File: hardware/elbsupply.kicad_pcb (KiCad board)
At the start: 2 copper layers, 105 x 64.4 mm, 86 parts, among them CON1 AVR-ISP-6, IC1 ATMEGA8-AI, M3 Screw_PAN_Head_M3, P1 OUT_POS, P2 OUT_GND, P3 POWER_IN, Q1 KST2907A, SW1 SW_L, SW2 SW_R, SW3 SW_OE, SW4 SW_MD, U1 LM393, U2 TPS54331DDA, U3 LT1490, U4 LM358, U5 TS78L05CS, U6 LT3083

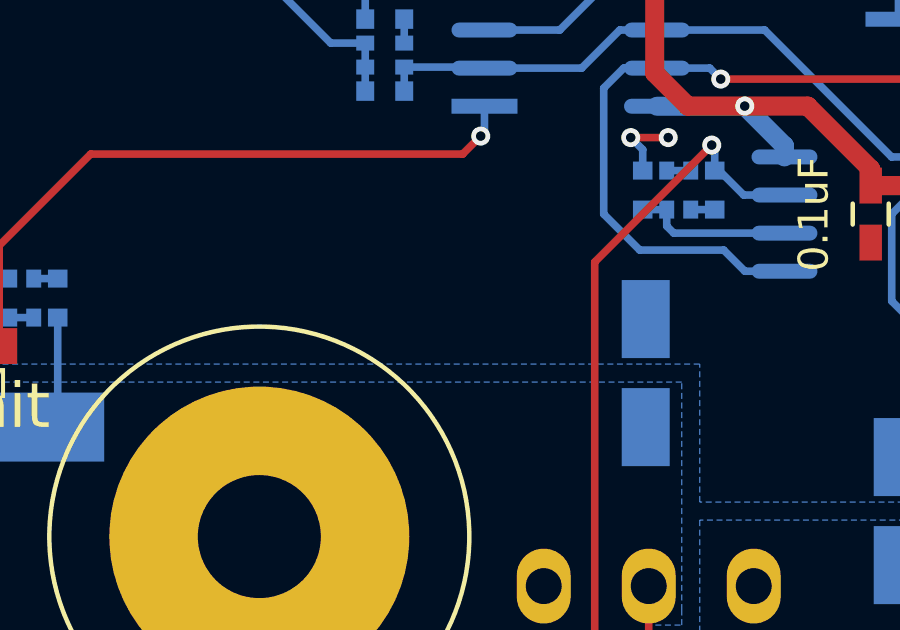
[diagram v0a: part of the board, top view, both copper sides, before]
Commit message: quickly added LM334 constant current sink to ensure stable operation of LT3083
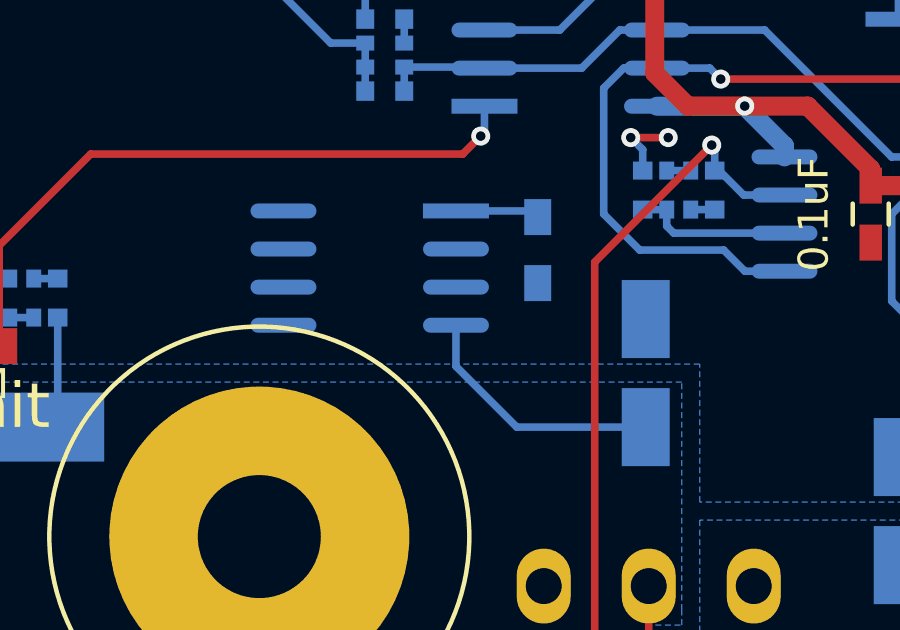
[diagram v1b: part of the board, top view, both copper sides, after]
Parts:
- added R26: R, Resistors_SMD:R_0603_HandSoldering, B.Cu at (80.4, 73.0)
- added U7: LM334, devthrash_KICAD:SO8, B.Cu at (74.8, 73.6)
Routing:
- net /LIN_OUT: track 37.8 -> 46.3 mm
- net Net-(R26-Pad1): track 0.00 -> 2.81 mm

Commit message: started new layout
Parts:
- added C28: 1uF, Capacitors_SMD:C_0805_HandSoldering, B.Cu at (101.4, 172.1)
- added D6: LM4040, Housings_SOT-23_SOT-143_TSOT-6:SOT-23_Handsoldering, B.Cu at (74.1, 60.7)
- added D7: SK34A, SMD_Packages:DO-214-AC_SMA, F.Cu at (63.6, 108.0)
- added D8: SK34A, SMD_Packages:DO-214-AC_SMA, B.Cu at (61.7, 82.7)
- added HS1: HEATSINK V5640A, devthrash:Heatsink-V5640A, B.Cu at (71.1, 77.7)
- added L2: 220uH, devthrash:242418FPS-Fastron, B.Cu at (115.4, 63.9)
- added Q2: KST2907A, Housings_SOT-23_SOT-143_TSOT-6:SOT-23_Handsoldering, B.Cu at (181.5, 107.1)
- added Q3: IRLML6302, Housings_SOT-23_SOT-143_TSOT-6:SOT-23_Handsoldering, B.Cu at (185.3, 107.1)
- added Q4: 2N2222A, Housings_SOT-23_SOT-143_TSOT-6:SOT-23_Handsoldering, B.Cu at (101.8, 169.2)
- added Q5: 2N2222A, Housings_SOT-23_SOT-143_TSOT-6:SOT-23_Handsoldering, F.Cu at (73.4, 117.0)
- added R27: 10k, Resistors_SMD:R_0603_HandSoldering, F.Cu at (63.1, 135.5)
- added R28: 10k, Resistors_SMD:R_0603_HandSoldering, F.Cu at (70.2, 138.9)
- added R29: 10k, Resistors_SMD:R_0603_HandSoldering, F.Cu at (73.5, 144.0)
- added RP6: 10k, devthrash:YC164-Yageo-Handsoldering, B.Cu at (98.5, 162.8)
- added RP7: 10k, devthrash:YC164-Yageo-Handsoldering, B.Cu at (102.6, 162.8)
- C10: value 10nF -> 120pF
- C11: value 10nF -> 10uF; footprint Capacitors_SMD:C_0603_HandSoldering -> Capacitors_SMD:c_elec_4x4.5
- C12: value 10nF -> 10uF; footprint Capacitors_SMD:C_0603_HandSoldering -> Capacitors_SMD:C_0805_HandSoldering
- C13, C17, C18, C19, C23: footprint Capacitors_SMD:C_0603_HandSoldering -> Capacitors_SMD:C_0805_HandSoldering
- C14, C21: value 0.1uF -> 1uF; footprint Capacitors_SMD:C_0603_HandSoldering -> Capacitors_SMD:C_0805_HandSoldering
- C20: value 10uF -> 1uF; footprint Capacitors_SMD:c_elec_4x4.5 -> Capacitors_SMD:C_0805_HandSoldering; moved to F.Cu
- C22: footprint Capacitors_SMD:C_0603_HandSoldering -> Capacitors_SMD:C_0805_HandSoldering; moved to B.Cu
- C25: moved to B.Cu
- C26, R3: moved to F.Cu
- C4: value 7pF -> 22pF
- C7, C9: value 10nF -> 0.1uF; footprint Capacitors_SMD:C_0603_HandSoldering -> Capacitors_SMD:C_0805_HandSoldering
- D5: value SM6T27A -> SK34A; footprint Diodes_SMD:Diode-SMB_Handsoldering -> SMD_Packages:DO-214-AC_SMA
- DS1: footprint devthrash_KICAD:LCD16X2 -> devthrash:LCD16X2
- R1: value 102k -> 100k
- R14: value 10k -> 3k9
- R16: value 10k -> 220; moved to F.Cu
- R20, R25: value 10k -> 1k
- R21: value 1k -> 10R
- R23: value 220 -> 10k
- R24: value 10k -> 100
- R26: value R -> 10R; footprint Resistors_SMD:R_0603_HandSoldering -> Resistors_SMD:R_0805_HandSoldering; moved to F.Cu
- R4: value 10k -> 33k; moved to F.Cu
- R5: value 10k -> 1R; footprint Resistors_SMD:R_0603_HandSoldering -> Resistors_SMD:R_0805_HandSoldering
- R6: value 10k -> 18k
- R7: value 1k -> 10k
- R8: value 18k -> 33k
- RP1, RP5: footprint devthrash_KICAD:YC164-Yageo -> devthrash:YC164-Yageo-Handsoldering; moved to F.Cu
- RP2, RP3, RP4: footprint devthrash_KICAD:YC164-Yageo -> devthrash:YC164-Yageo-Handsoldering
- U1: value LM393 -> MC34063; footprint devthrash_KICAD:SO8 -> devthrash:SO8
- U3: value LT1490 -> LM324; footprint devthrash_KICAD:SO8 -> devthrash:SO14
- U4: footprint devthrash_KICAD:SO8 -> devthrash:SO8
- U6: value LT3083 -> LM350T; footprint Pentawatts:Pentawatt_Neutral_Staggered_Verical_TO220-5-T05D -> Power_Integrations:TO-220
- U7: footprint devthrash_KICAD:SO8 -> devthrash:SO8; moved to F.Cu
- moved R23 131.3 mm to (104.4, 166.4)
- moved R24 126.5 mm to (97.8, 170.3), turned to 90 degrees
- moved R25 122.1 mm to (107.1, 169.2), turned to 0 degrees
- moved C25 117.1 mm to (105.8, 162.9)
- moved C23 109.2 mm to (78.1, 166.3), turned to 0 degrees
- moved C14 106.9 mm to (62.5, 165.0), turned to 180 degrees
- moved R21 104.9 mm to (181.5, 110.9), turned to 0 degrees
- moved R7 104.7 mm to (61.9, 161.7), turned to 270 degrees
- moved R11 103.8 mm to (63.8, 161.7)
- moved C21 103.6 mm to (76.5, 160.9)
- moved U4 103.4 mm to (69.7, 163.6)
- moved C13 102.6 mm to (62.5, 158.4)
- moved R19 102.5 mm to (113.2, 168.1)
- moved C9 101.6 mm to (110.0, 155.6), turned to 90 degrees
- moved C7 100.3 mm to (112.7, 155.6), turned to 90 degrees
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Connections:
- C1 pad 2: +24V -> VCC
- C10 pad 1: /SW_OE -> Net-(C10-Pad1)
- C10 pad 2: GND -> VEE
- C11 pad 1: /SW_MD -> VCC
- C12 pad 2: /ENC_SW -> VEE
- C15 pad 1: GND -> /ENC_A
- C15 pad 2: /ENC_A -> GND
- C17 pad 1: +24V -> VEE
- C18 pad 1: +24V -> VCC
- C2 pad 2: +24V -> VCC
- C20 pad 1: /LIN_IN -> /2.5VREF
- C22 pad 1: +24V -> VCC
- C25 pad 1: Net-(C25-Pad1) -> /I_Meas
- C7 pad 1: /SW_L -> VCC
- C9 pad 1: /SW_R -> VEE
- D5 pad 1: /LIN_OUT -> VEE
- D5 pad 2: GND -> Net-(D5-Pad2)
- DS1 pad 10: /LCD_D3 -> Net-(DS1-Pad10)
- DS1 pad 11: Net-(DS1-Pad11) -> /LCD_D4
- DS1 pad 12: Net-(DS1-Pad12) -> /LCD_D5
- DS1 pad 13: Net-(DS1-Pad13) -> /LCD_D6
- DS1 pad 14: Net-(DS1-Pad14) -> /LCD_D7
- DS1 pad 7: /LCD_D0 -> Net-(DS1-Pad7)
- DS1 pad 8: /LCD_D1 -> Net-(DS1-Pad8)
- DS1 pad 9: /LCD_D2 -> Net-(DS1-Pad9)
- IC1 pad 2: /ENC_A -> /ENC_SW
- IC1 pad 20: Net-(C25-Pad1) -> /2.5VREF
- IC1 pad 25: /LCD_D0 -> /LCD_D4
- IC1 pad 26: /LCD_D1 -> /LCD_D5
- IC1 pad 27: /LCD_D2 -> /LCD_D6
- IC1 pad 28: /LCD_D3 -> /LCD_D7
- IC1 pad 30: Net-(IC1-Pad30) -> /SW_L
- IC1 pad 31: Net-(IC1-Pad31) -> /SW_R
- IC1 pad 32: /ENC_SW -> /ENC_A
- IC1 pad 7: /SW_L -> Net-(IC1-Pad7)
- IC1 pad 8: /SW_R -> Net-(IC1-Pad8)
- P3 pad 2: +24V -> VCC
- R1 pad 1: Net-(C5-Pad2) -> Net-(R1-Pad1)
- R14 pad 1: +5V -> VEE
- R14 pad 2: /ENC_A -> Net-(R14-Pad2)
- R16 pad 2: /ENC_B -> /2.5VREF
- R17 pad 1: /LIN_IN -> Net-(R17-Pad1)
- R18 pad 1: /I_Meas -> Net-(R18-Pad1)
- R19 pad 1: /V_control -> /I_Meas
- R19 pad 2: /V_Set -> Net-(R18-Pad1)
- R20 pad 1: Net-(C21-Pad1) -> Net-(Q2-Pad3)
- R20 pad 2: Net-(C23-Pad1) -> GND
- R21 pad 1: Net-(C23-Pad1) -> VCC
- R21 pad 2: /V_PWM -> Net-(Q2-Pad1)
- R23 pad 1: +24V -> /ILIM
- R23 pad 2: Net-(DS1-Pad15) -> Net-(Q4-Pad1)
- R24 pad 1: +5V -> Net-(C28-Pad1)
- R24 pad 2: /SW_OE -> Net-(Q4-Pad3)
- R25 pad 1: +5V -> Net-(Q4-Pad3)
- R25 pad 2: /SW_MD -> Net-(R25-Pad2)
- R26 pad 2: GND -> VEE
- R4 pad 1: +5V -> Net-(C5-Pad2)
- R4 pad 2: /SW_L -> Net-(R1-Pad1)
- R5 pad 1: +5V -> Net-(R5-Pad1)
- R5 pad 2: /SW_R -> VCC
- R6 pad 1: +5V -> Net-(R14-Pad2)
- R6 pad 2: /ENC_SW -> GND
- RP2 pad 2: Net-(RP2-Pad1) -> Net-(RP2-Pad2)
- RP2 pad 3: Net-(RP2-Pad3) -> Net-(RP2-Pad2)
- RP2 pad 4: Net-(RP2-Pad3) -> Net-(RP2-Pad4)
- RP2 pad 5: GND -> Net-(RP2-Pad5)
- RP2 pad 6: Net-(RP2-Pad6) -> Net-(RP2-Pad5)
- RP2 pad 7: Net-(RP2-Pad6) -> Net-(C28-Pad1)
- RP4 pad 1: /LIN_OUT -> Net-(RP4-Pad1)
- RP4 pad 2: Net-(RP4-Pad2) -> Net-(RP4-Pad1)
- RP4 pad 3: Net-(RP4-Pad2) -> Net-(C21-Pad1)
- RP4 pad 4: Net-(RP4-Pad4) -> Net-(C21-Pad1)
- RP4 pad 5: Net-(RP4-Pad5) -> /V_PWM
- RP4 pad 6: Net-(RP4-Pad5) -> Net-(C23-Pad1)
- RP4 pad 7: Net-(RP4-Pad7) -> Net-(C23-Pad1)
- RP4 pad 8: Net-(RP4-Pad7) -> /V_Set
- RP5 pad 1: Net-(RP4-Pad4) -> /LIN_OUT
- RP5 pad 4: GND -> Net-(R28-Pad1)
- RP5 pad 5: /V_ADC -> Net-(RP5-Pad5)
- RP5 pad 6: /V_ADC -> Net-(RP5-Pad5)
- U1 pad 1: Net-(D1-Pad2) -> Net-(R5-Pad1)
- U1 pad 2: /I_Meas -> Net-(D5-Pad2)
- U1 pad 3: /I_Set -> Net-(C10-Pad1)
- U1 pad 4: GND -> VEE
- U1 pad 5: /I_Set -> Net-(R14-Pad2)
- U1 pad 6: /I_Meas -> VCC
- U1 pad 7: /V_control -> Net-(R5-Pad1)
- U1 pad 8: +24V -> Net-(R5-Pad1)
- U2 pad 2: +24V -> VCC
- U3 pad 1: /I_Meas -> Net-(R17-Pad1)
- U3 pad 2: Net-(R17-Pad2) -> Net-(R17-Pad1)
- U3 pad 3: Net-(R12-Pad1) -> /LIN_IN
- U3 pad 4: GND -> VCC
- U3 pad 5: /V_control -> Net-(R12-Pad1)
- U3 pad 6: Net-(RP2-Pad3) -> Net-(R17-Pad2)
- U3 pad 7: Net-(RP2-Pad8) -> Net-(R18-Pad1)
- U3 pad 8: +24V -> /ILIM
- U4 pad 4: GND -> VEE
- U4 pad 5: Net-(C21-Pad1) -> GND
- U4 pad 6: /V_Set -> Net-(RP4-Pad1)
- U4 pad 8: +24V -> VCC
- U5 pad 8: +24V -> VCC
- U6 pad 1: Net-(U6-Pad1) -> Net-(C28-Pad1)
- U6 pad 2: Net-(RP2-Pad8) -> /LIN_OUT
- U6 pad 3: /LIN_OUT -> /LIN_IN
- U7 pad 2: GND -> VEE
- U7 pad 3: GND -> VEE
- U7 pad 6: GND -> VEE
- U7 pad 7: GND -> VEE
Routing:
- net +24V: track 218.9 -> 0.00 mm, vias 4 -> 0
- net VCC: track 0.00 -> 141.3 mm, vias 0 -> 1
- net /SW_OE: track 88.9 -> 0.00 mm, vias 3 -> 0
- net /SW_MD: track 88.2 -> 0.25 mm, vias 3 -> 0
- net /SW_R: track 70.3 -> 0.00 mm, vias 1 -> 0
- net /ENC_SW: track 67.0 -> 0.00 mm, vias 1 -> 0
- net /ENC_B: track 66.0 -> 0.64 mm, vias 1 -> 0
- net /SW_L: track 61.4 -> 0.00 mm, vias 1 -> 0
- net /ENC_A: track 60.4 -> 0.14 mm, vias 1 -> 0
- net /LIN_OUT: track 46.3 -> 0.00 mm, vias 1 -> 0
- net +5V: track 145.8 -> 106.4 mm
- net /I_Meas: track 31.7 -> 0.00 mm
- net /V_ADC: track 28.0 -> 0.00 mm
- net /V_control: track 23.1 -> 0.00 mm, vias 2 -> 0
- net Net-(RP2-Pad8): track 22.9 -> 0.00 mm, vias 1 -> 0
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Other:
- board text added: "Rev. B"
- board text removed: "Rev. A"

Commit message: continued board layout
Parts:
- C17, C22, C7, C9: moved to F.Cu
- C26, D7, R16, R26, R28, R29, R3, RP1, RP5, U7: moved to B.Cu
- moved Q3 115.4 mm to (87.7, 45.6)
- moved R21 115.2 mm to (84.2, 49.3)
- moved Q2 115.1 mm to (84.2, 45.6)
- moved R7 111.3 mm to (96.0, 55.7), turned to 180 degrees
- moved C14 109.6 mm to (93.6, 59.9)
- moved R11 108.2 mm to (97.1, 58.8)
- moved C22 106.5 mm to (97.1, 64.1), turned to 90 degrees
- moved R20 106.1 mm to (90.6, 46.0), turned to 90 degrees
- moved C13 105.4 mm to (93.6, 57.7), turned to 180 degrees
- moved C21 103.6 mm to (102.4, 60.6)
- moved C28 103.4 mm to (80.9, 70.8), turned to 180 degrees
- moved U4 102.9 mm to (96.0, 64.1)
- moved RP4 102.9 mm to (102.5, 64.1)
- moved C23 102.4 mm to (103.4, 67.1)
- moved R19 99.6 mm to (95.2, 70.1)
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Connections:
- U3 pad 1: Net-(R17-Pad1) -> Net-(R18-Pad1)
- U3 pad 2: Net-(R17-Pad1) -> Net-(R17-Pad2)
- U3 pad 3: /LIN_IN -> Net-(R12-Pad1)
- U3 pad 5: Net-(R12-Pad1) -> /LIN_IN
- U3 pad 6: Net-(R17-Pad2) -> Net-(R17-Pad1)
- U3 pad 7: Net-(R18-Pad1) -> Net-(R17-Pad1)
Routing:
- net +5V: track 106.4 -> 42.0 mm, vias 2 -> 1
- net /LCD_D7: track 0.00 -> 38.6 mm
- net /LCD_D6: track 0.00 -> 36.4 mm
- net /LCD_D5: track 0.00 -> 34.8 mm
- net /MISO: track 41.7 -> 7.06 mm, vias 1 -> 0
- net /LCD_D4: track 0.00 -> 32.6 mm
- net /SCK: track 40.3 -> 9.34 mm
- net /MOSI: track 44.2 -> 21.2 mm
- net /I_Meas: track 0.00 -> 21.4 mm, vias 0 -> 2
- net Net-(D1-Pad1): track 18.8 -> 0.00 mm
- net /I_Set: track 0.00 -> 17.5 mm
- net Net-(RP2-Pad4): track 0.00 -> 15.2 mm
- net /LCD_E: track 14.1 -> 28.3 mm
- net GND: track 51.2 -> 39.1 mm, vias 29 -> 22
- net Net-(C28-Pad1): track 0.00 -> 9.30 mm
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- added copper zone on B.Cu, net VCC
- removed copper zone on B.Cu, net +24V

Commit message: RevB layout finished
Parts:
- moved D5 7.00 mm to (121.6, 57.6)
- moved L2 6.32 mm to (121.6, 65.1), turned to 270 degrees
- moved C12 6.22 mm to (125.6, 55.9), turned to 270 degrees
- moved R2 5.14 mm to (89.2, 78.6), turned to 180 degrees
- moved R21 4.96 mm to (85.8, 54.0), turned to 180 degrees
- moved Q2 4.87 mm to (85.8, 50.2), turned to 0 degrees
- moved C23 4.28 mm to (106.0, 63.7), turned to 90 degrees
- moved R14 4.27 mm to (130.9, 57.6)
- moved C10 4.24 mm to (125.6, 60.2)
- moved R6 4.23 mm to (133.9, 56.4)
- moved U1 4.14 mm to (131.1, 61.9)
- moved R5 3.65 mm to (138.0, 63.7)
- moved C11 3.20 mm to (138.3, 59.2)
- moved Q3 3.10 mm to (84.8, 44.5)
- moved R20 3.10 mm to (87.7, 44.9)
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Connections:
- net Net-(D5-Pad2) renamed /MC34_Emit
- net Net-(DS1-Pad15) renamed /LED_CC
- net Net-(Q2-Pad1) renamed /LED_CS
- net Net-(R5-Pad1) renamed /MC34_Coll
- D2 pad 1: Net-(D2-Pad1) -> GND
- D2 pad 2: GND -> Net-(D2-Pad2)
- IC1 pad 10: /SW_OE -> /SW_MD
- IC1 pad 9: /SW_MD -> /SW_OE
- Q5 pad 3: Net-(D1-Pad2) -> Net-(D1-Pad1)
- R2 pad 1: +5V -> VCC
- R2 pad 2: Net-(D1-Pad1) -> Net-(D1-Pad2)
- R3 pad 2: Net-(D2-Pad1) -> Net-(D2-Pad2)
- RP7 pad 1: Net-(RP7-Pad1) -> /V_Set
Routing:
- net +5V: track 42.0 -> 184.0 mm, vias 1 -> 3
- net VEE: track 0.00 -> 107.7 mm, vias 0 -> 5
- net /SW_OE: track 0.00 -> 94.4 mm, vias 0 -> 1
- net /SW_MD: track 0.25 -> 90.4 mm, vias 0 -> 1
- net /ENC_SW: track 0.00 -> 87.4 mm, vias 0 -> 1
- net /SW_R: track 0.00 -> 87.3 mm, vias 0 -> 1
- net /ENC_B: track 0.64 -> 81.5 mm, vias 0 -> 1
- net VCC: track 143.6 -> 221.5 mm, vias 1 -> 5
- net /ENC_A: track 0.14 -> 76.8 mm, vias 0 -> 1
- net /SW_L: track 0.00 -> 76.2 mm, vias 0 -> 1
- net /I_ADC: track 0.00 -> 66.8 mm, vias 0 -> 2
- net /I_PWM: track 0.00 -> 60.9 mm, vias 0 -> 2
- net /V_PWM: track 0.00 -> 54.4 mm, vias 0 -> 2
- net /LIN_OUT: track 8.43 -> 58.5 mm
- net /2.5VREF: track 7.82 -> 47.0 mm, vias 1 -> 3
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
